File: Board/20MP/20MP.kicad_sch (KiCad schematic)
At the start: 49 parts, among them J1 Conn_01x02_Male, SW1 SHOU_HAN_MSK12C02-HB, SW2 RotaryEncoder_Switch, U1 nice_nanoV2

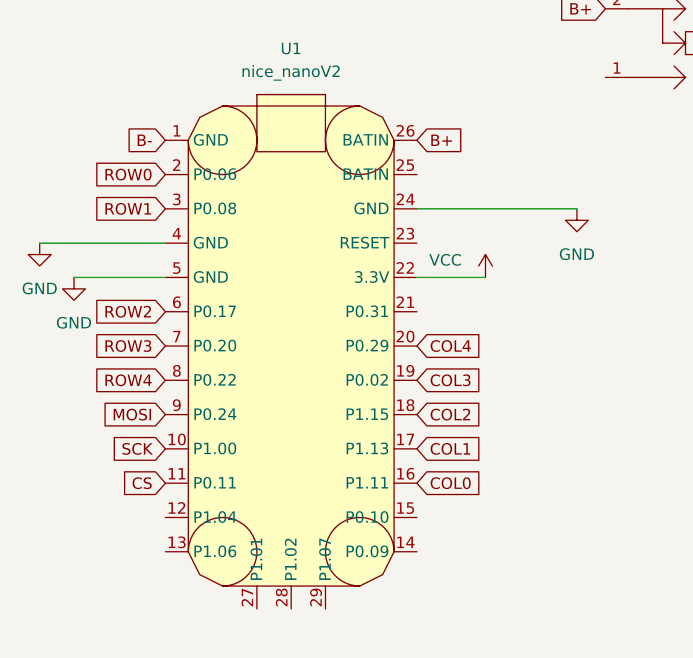
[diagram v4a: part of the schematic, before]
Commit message: changed oled wiring
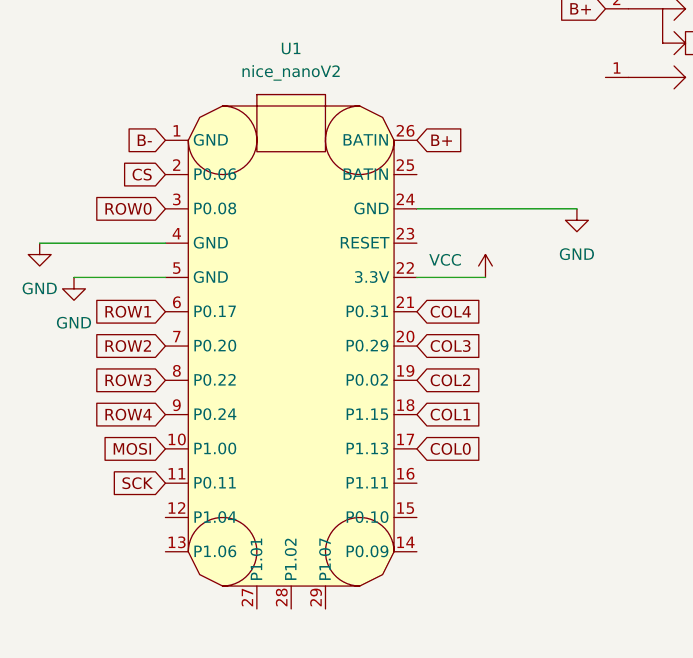
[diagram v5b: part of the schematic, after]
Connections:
- net COL0: now also U1.17 (P1.13); no longer U1.16 (P1.11)
- net COL1: now also U1.18 (P1.15); no longer U1.17 (P1.13)
- net COL2: now also U1.19 (P0.02); no longer U1.18 (P1.15)
- net COL3: now also U1.20 (P0.29); no longer U1.19 (P0.02)
- net COL4: now also U1.21 (P0.31); no longer U1.20 (P0.29)
- net CS: now also U1.2 (P0.06); no longer U1.11 (P0.11)
- net MOSI: now also U1.10 (P1.00); no longer U1.9 (P0.24)
- net ROW0: now also U1.3 (P0.08); no longer U1.2 (P0.06)
- net ROW1: now also U1.6 (P0.17); no longer U1.3 (P0.08)
- net ROW2: now also U1.7 (P0.20); no longer U1.6 (P0.17)
- net ROW3: now also U1.8 (P0.22); no longer U1.7 (P0.20)
- net ROW4: now also U1.9 (P0.24); no longer U1.8 (P0.22)
- net SCK: now also U1.11 (P0.11); no longer U1.10 (P1.00)
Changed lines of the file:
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@@
     (effects (font (size 1.27 1.27)) (justify left bottom))
   )
-  (global_label "COL1" (shape input) (at 91.44 101.6 0) (fields_autoplaced)
+  (global_label "COL1" (shape input) (at 91.44 97.79 0) (fields_autoplaced)
+    (effects (font (size 1.27 1.27)) (justify left))
+    (property "Intersheet References" "${INTERSHEET_REFS}" (id 0) (at 98.6912 97.7106 0)
+      (effects (font (size 1.27 1.27)) (justify left) hide)
+    )
+  )
+  (global_label "COL0" (shape input) (at 91.44 101.6 0) (fields_autoplaced)
     (effects (font (size 1.27 1.27)) (justify left))
     (property "Intersheet References" "${INTERSHEET_REFS}" (id 0) (at 98.6912 101.5206 0)
@@
     )
   )
-  (global_label "COL0" (shape input) (at 91.44 105.41 0) (fields_autoplaced)
-    (effects (font (size 1.27 1.27)) (justify left))
-    (property "Intersheet References" "${INTERSHEET_REFS}" (id 0) (at 98.6912 105.3306 0)
-      (effects (font (size 1.27 1.27)) (justify left) hide)
-    )
-  )
-  (global_label "ROW1" (shape input) (at 63.5 74.93 180) (fields_autoplaced)
+  (global_label "ROW1" (shape input) (at 63.5 86.36 180) (fields_autoplaced)
     (effects (font (size 1.27 1.27)) (justify right))
-    (property "Intersheet References" "${INTERSHEET_REFS}" (id 0) (at 55.8255 74.8506 0)
+    (property "Intersheet References" "${INTERSHEET_REFS}" (id 0) (at 55.8255 86.2806 0)
       (effects (font (size 1.27 1.27)) (justify right) hide)
     )
@@
     )
   )
-  (global_label "ROW0" (shape input) (at 63.5 71.12 180) (fields_autoplaced)
+  (global_label "ROW0" (shape input) (at 63.5 74.93 180) (fields_autoplaced)
     (effects (font (size 1.27 1.27)) (justify right))
-    (property "Intersheet References" "${INTERSHEET_REFS}" (id 0) (at 55.8255 71.0406 0)
+    (property "Intersheet References" "${INTERSHEET_REFS}" (id 0) (at 55.8255 74.8506 0)
       (effects (font (size 1.27 1.27)) (justify right) hide)
     )
   )
-  (global_label "CS" (shape input) (at 63.5 105.41 180) (fields_autoplaced)
+  (global_label "CS" (shape input) (at 63.5 71.12 180) (fields_autoplaced)
     (effects (font (size 1.27 1.27)) (justify right))
-    (property "Intersheet References" "${INTERSHEET_REFS}" (id 0) (at 58.6074 105.3306 0)
+    (property "Intersheet References" "${INTERSHEET_REFS}" (id 0) (at 58.6074 71.0406 0)
       (effects (font (size 1.27 1.27)) (justify right) hide)
     )
@@
     )
   )
-  (global_label "SCK" (shape input) (at 63.5 101.6 180) (fields_autoplaced)
+  (global_label "SCK" (shape input) (at 63.5 105.41 180) (fields_autoplaced)
     (effects (font (size 1.27 1.27)) (justify right))
-    (property "Intersheet References" "${INTERSHEET_REFS}" (id 0) (at 57.3374 101.5206 0)
+    (property "Intersheet References" "${INTERSHEET_REFS}" (id 0) (at 57.3374 105.3306 0)
       (effects (font (size 1.27 1.27)) (justify right) hide)
     )
@@
     )
   )
-  (global_label "ROW2" (shape input) (at 63.5 86.36 180) (fields_autoplaced)
+  (global_label "ROW2" (shape input) (at 63.5 90.17 180) (fields_autoplaced)
     (effects (font (size 1.27 1.27)) (justify right))
-    (property "Intersheet References" "${INTERSHEET_REFS}" (id 0) (at 55.8255 86.2806 0)
+    (property "Intersheet References" "${INTERSHEET_REFS}" (id 0) (at 55.8255 90.0906 0)
       (effects (font (size 1.27 1.27)) (justify right) hide)
     )
   )
-  (global_label "COL2" (shape input) (at 91.44 97.79 0) (fields_autoplaced)
+  (global_label "COL2" (shape input) (at 91.44 93.98 0) (fields_autoplaced)
     (effects (font (size 1.27 1.27)) (justify left))
-    (property "Intersheet References" "${INTERSHEET_REFS}" (id 0) (at 98.6912 97.7106 0)
+    (property "Intersheet References" "${INTERSHEET_REFS}" (id 0) (at 98.6912 93.9006 0)
       (effects (font (size 1.27 1.27)) (justify left) hide)
     )
   )
-  (global_label "ROW3" (shape input) (at 63.5 90.17 180) (fields_autoplaced)
+  (global_label "ROW3" (shape input) (at 63.5 93.98 180) (fields_autoplaced)
     (effects (font (size 1.27 1.27)) (justify right))
-    (property "Intersheet References" "${INTERSHEET_REFS}" (id 0) (at 55.8255 90.0906 0)
+    (property "Intersheet References" "${INTERSHEET_REFS}" (id 0) (at 55.8255 93.9006 0)
       (effects (font (size 1.27 1.27)) (justify right) hide)
     )
@@
     )
   )
-  (global_label "ROW4" (shape input) (at 63.5 93.98 180) (fields_autoplaced)
+  (global_label "ROW4" (shape input) (at 63.5 97.79 180) (fields_autoplaced)
     (effects (font (size 1.27 1.27)) (justify right))
-    (property "Intersheet References" "${INTERSHEET_REFS}" (id 0) (at 55.8255 93.9006 0)
+    (property "Intersheet References" "${INTERSHEET_REFS}" (id 0) (at 55.8255 97.7106 0)
       (effects (font (size 1.27 1.27)) (justify right) hide)
     )
   )
-  (global_label "MOSI" (shape input) (at 63.5 97.79 180) (fields_autoplaced)
+  (global_label "MOSI" (shape input) (at 63.5 101.6 180) (fields_autoplaced)
     (effects (font (size 1.27 1.27)) (justify right))
-    (property "Intersheet References" "${INTERSHEET_REFS}" (id 0) (at 56.4907 97.7106 0)
+    (property "Intersheet References" "${INTERSHEET_REFS}" (id 0) (at 56.4907 101.5206 0)
       (effects (font (size 1.27 1.27)) (justify right) hide)
     )
@@
     )
   )
-  (global_label "COL4" (shape input) (at 91.44 90.17 0) (fields_autoplaced)
+  (global_label "COL4" (shape input) (at 91.44 86.36 0) (fields_autoplaced)
     (effects (font (size 1.27 1.27)) (justify left))
-    (property "Intersheet References" "${INTERSHEET_REFS}" (id 0) (at 98.6912 90.0906 0)
+    (property "Intersheet References" "${INTERSHEET_REFS}" (id 0) (at 98.6912 86.2806 0)
       (effects (font (size 1.27 1.27)) (justify left) hide)
     )
@@
     )
   )
-  (global_label "COL3" (shape input) (at 91.44 93.98 0) (fields_autoplaced)
+  (global_label "COL3" (shape input) (at 91.44 90.17 0) (fields_autoplaced)
     (effects (font (size 1.27 1.27)) (justify left))
-    (property "Intersheet References" "${INTERSHEET_REFS}" (id 0) (at 98.6912 93.9006 0)
+    (property "Intersheet References" "${INTERSHEET_REFS}" (id 0) (at 98.6912 90.0906 0)
       (effects (font (size 1.27 1.27)) (justify left) hide)
     )

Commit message: finished pcb
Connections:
- net ROT_1A: now also U1.15 (P0.10)
- net ROT_1B: now also U1.16 (P1.11)
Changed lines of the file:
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@@
+    (effects (font (size 1.27 1.27)) (justify left bottom))
+  )
+  (label "ROT_1A" (at 91.44 109.22 0)
     (effects (font (size 1.27 1.27)) (justify left bottom))
   )
@@
     (effects (font (size 1.27 1.27)) (justify left bottom))
   )
+  (label "ROT_1B" (at 91.44 105.41 0)
+    (effects (font (size 1.27 1.27)) (justify left bottom))
+  )
